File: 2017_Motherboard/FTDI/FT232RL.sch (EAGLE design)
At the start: 14 parts, among them IC1 FT232RL

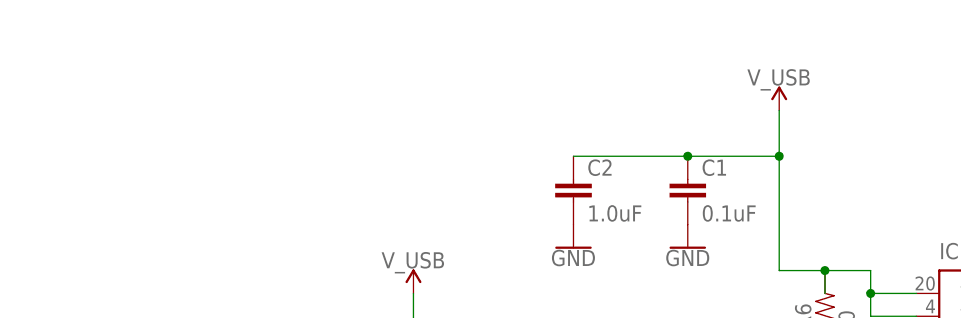
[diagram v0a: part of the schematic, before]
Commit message: Motherboard accelerometer + FTDI
updated to current FTDI and accelerometer on the schematic
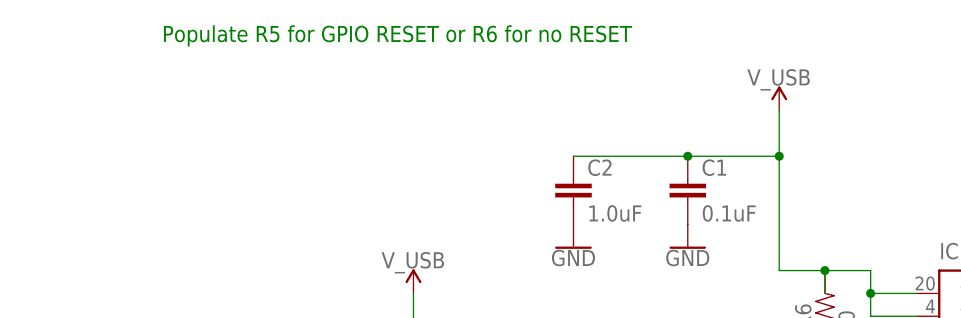
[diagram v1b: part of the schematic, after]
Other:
- note added: "Populate R5 for GPIO RESET or R6 for no RESET"
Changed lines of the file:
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@@
 Reviewed By:
 Version: 1.0</text>
+<text x="-27.94" y="96.52" size="1.778" layer="91">Populate R5 for GPIO RESET or R6 for no RESET</text>
 </plain>
 <instances>
